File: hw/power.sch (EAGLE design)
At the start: 18 parts, among them U1 TPS54200, U7 MIC5233

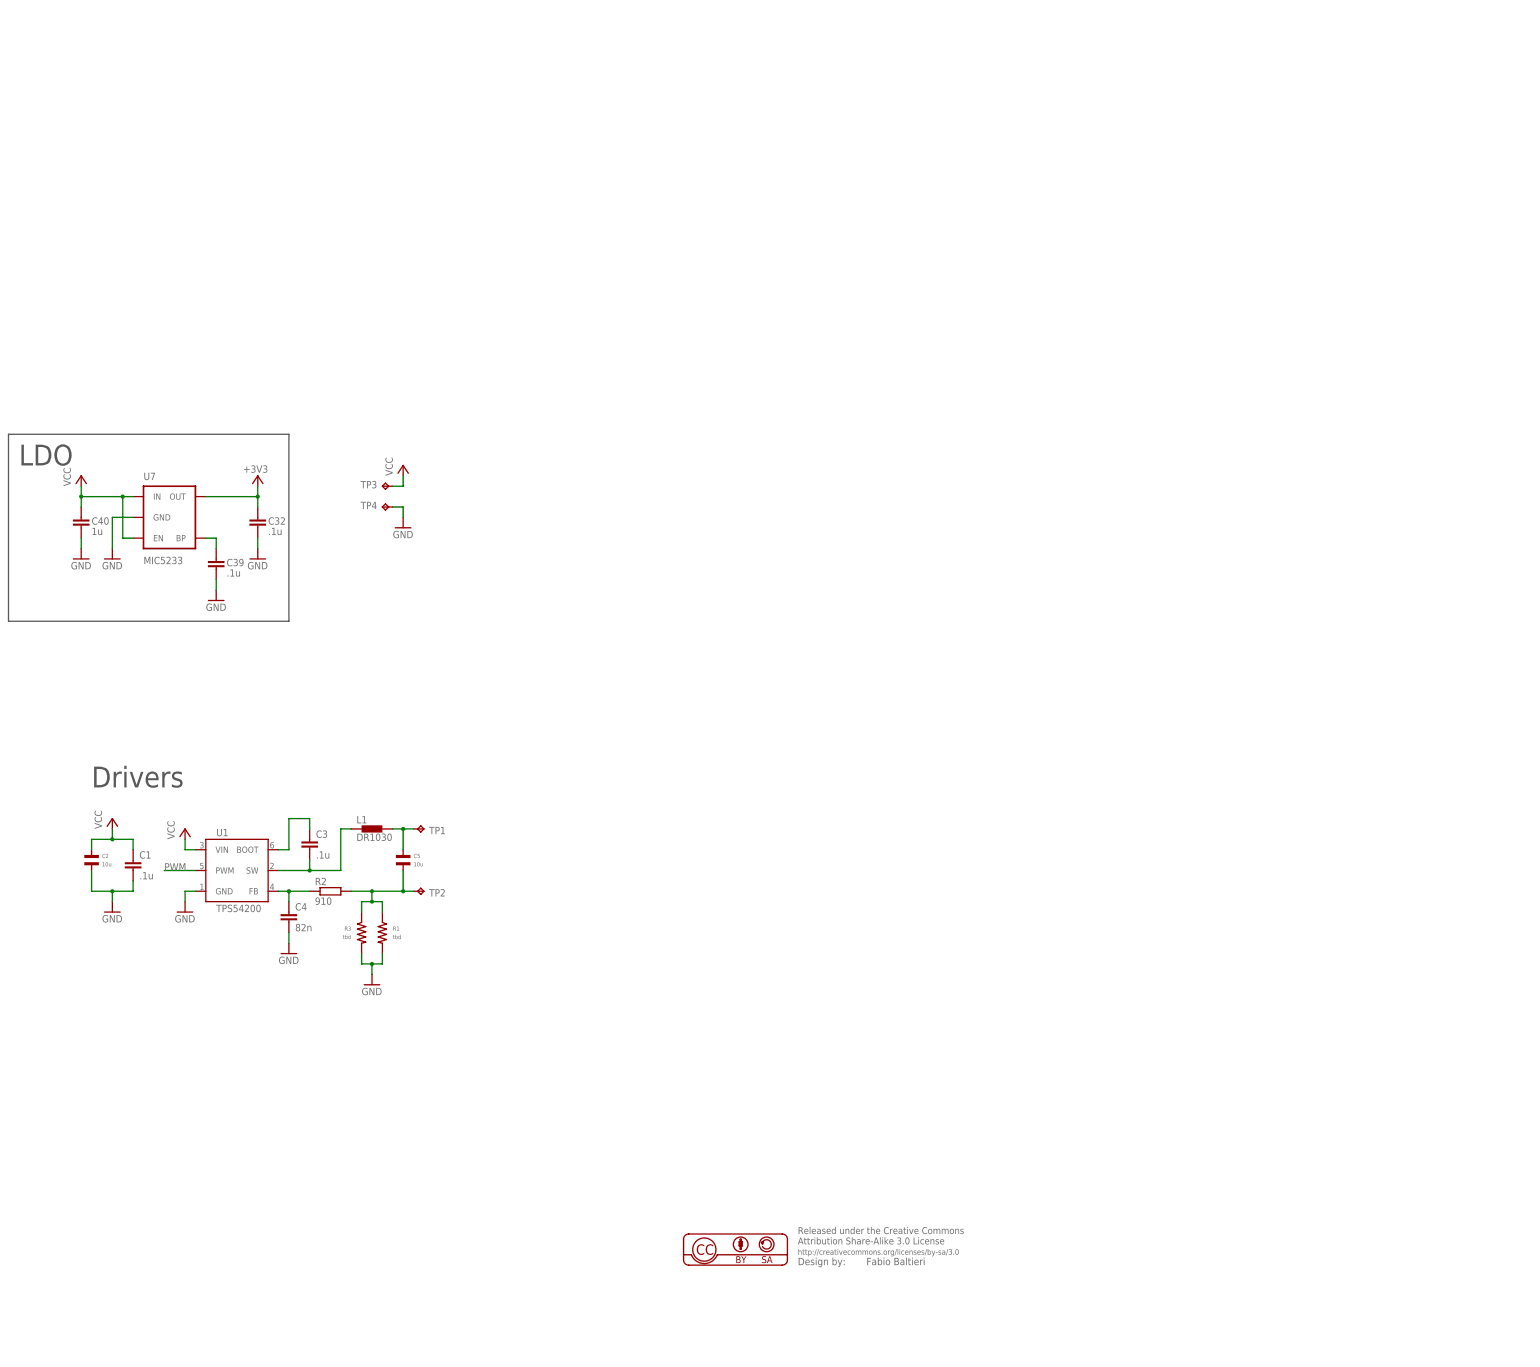
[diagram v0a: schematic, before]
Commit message: power: power routed, control placed
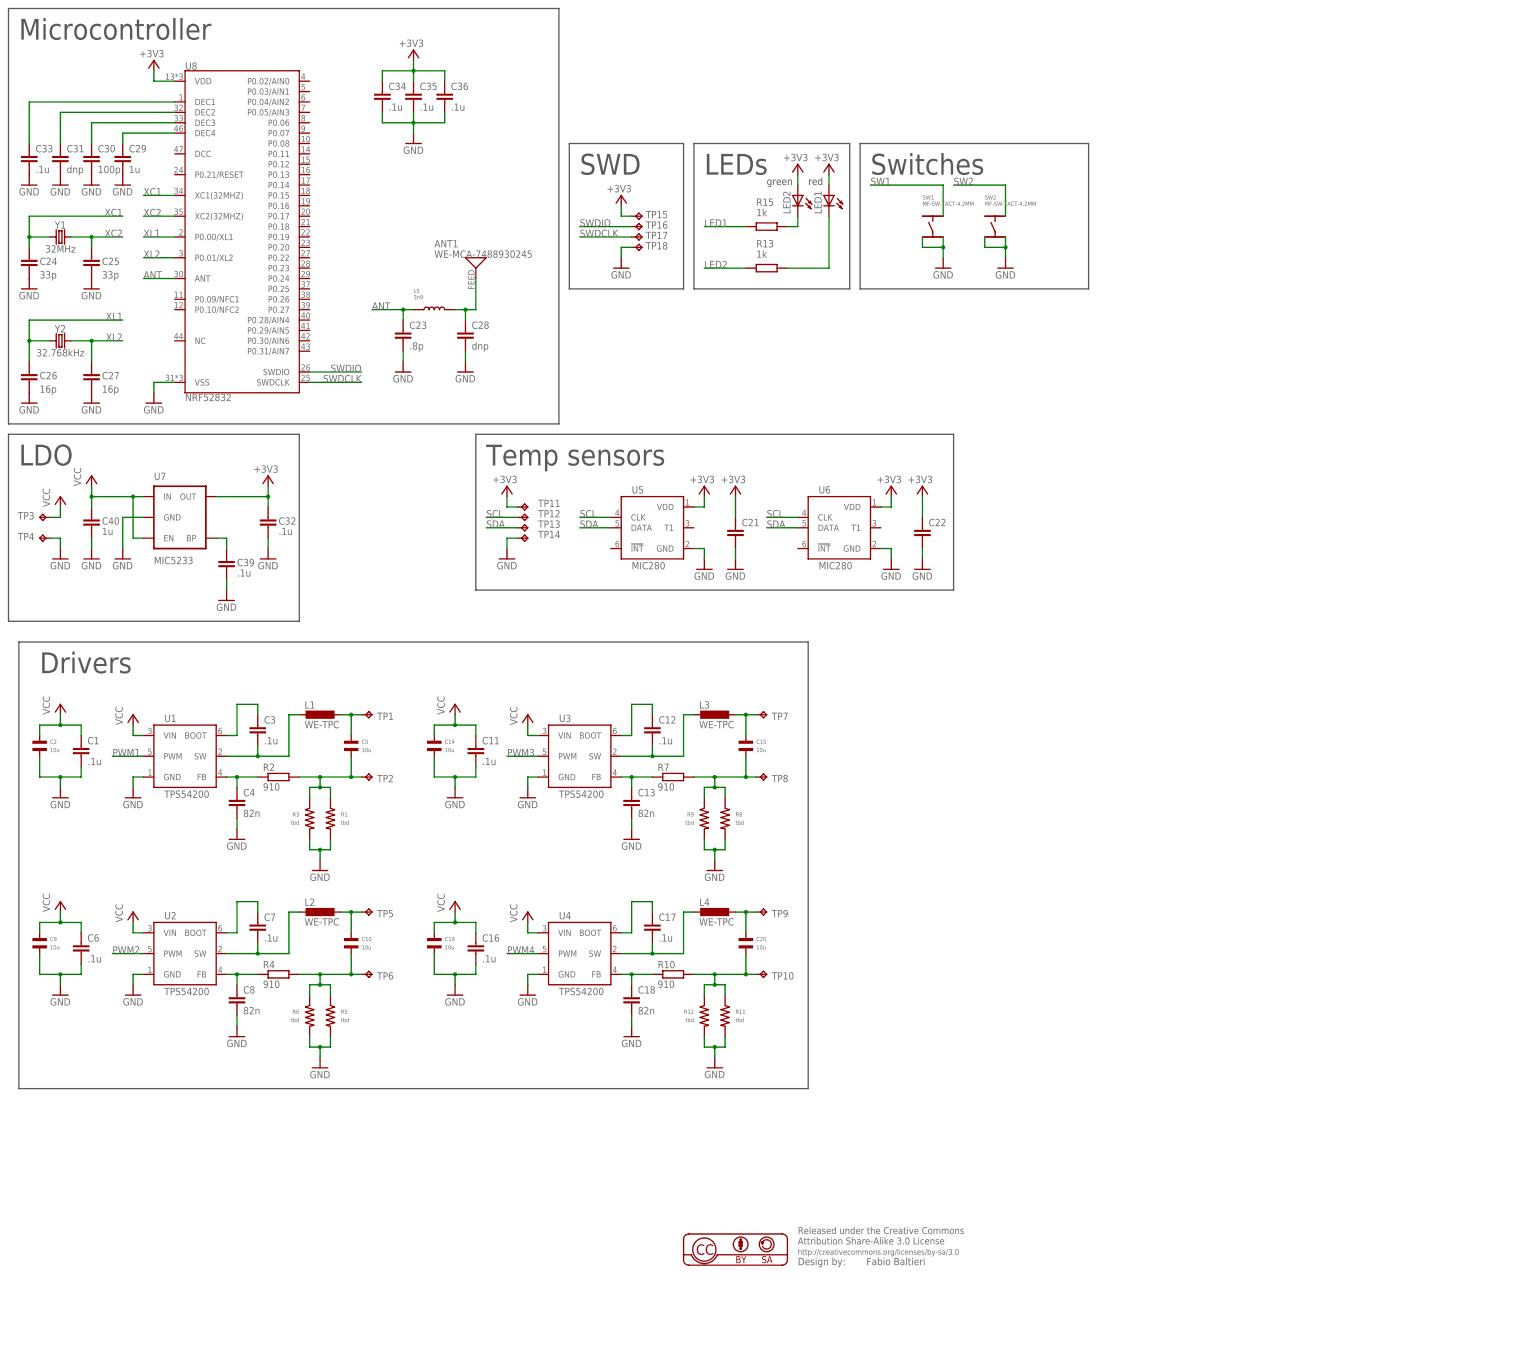
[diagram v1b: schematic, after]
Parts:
- added ANT1: WE-MCA-7488930245, balto:WE-MCA-7488930245
- added C10, C14, C15, C19, C20, C9: 10u, MF_Passives:CAPACITOR_NP_1206
- added C11, C12, C16, C17, C33, C34, C35, C36, C6, C7: .1u, balto:C0603
- added C13, C18, C8: 82n, balto:C0603
- added C21, C22: (no value), balto:C0603
- added C23: .8p, balto:C0603
- added C24, C25: 33p, balto:C0603
- added C26, C27: 16p, balto:C0603
- added C28, C31: dnp, balto:C0603
- added C29: 1u, balto:C0603
- added C30: 100p, balto:C0603
- added L2, L3, L4: WE-TPC, balto:WE-TPC
- added L5: 3n9, MF_Passives:INDUCTOR_0603
- added LED1, LED2: (no value), led:LEDSML0805
- added R10, R4, R7: 910, balto:R0603
- added R11, R12, R5, R6, R8, R9: tbd, MF_Passives:RESISTOR_0805
- added R13, R15: 1k, balto:R0603
- added SW1, SW2: MF-SW-TACT-4.2MM, MF_Switches:TACT_4.2MM
- added TP10, TP5, TP6, TP7, TP8, TP9: TPTP18R, testpad:TPTP18R
- added TP11, TP12, TP13, TP14: TPTP14R, testpad:TPTP14R
- added TP15, TP16, TP17, TP18: TPTP12R, testpad:TPTP12R
- added U2, U3, U4: TPS54200, balto:TPS54200
- added U5, U6: MIC280, balto:MIC280
- added U8: NRF52832, SparkFun-RF:NRF52832
- added Y1: 32MHz, SparkFun-Clocks:CRYSTALSMD-3.2X2.5
- added Y2: 32.768kHz, SparkFun-Clocks:CRYSTAL-32.768KHZSMD-3.2X1.5
- L1: value DR1030 -> WE-TPC; device inductors:DR1030 -> balto:WE-TPC
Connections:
- net PWM renamed PWM1
- new net ANT: C23.1, L5.P$1, U8.ANT
- new net LED1: R15.2
- new net LED2: R13.2
- new net N$10: C10.P$1, L2.2, TP5.TP
- new net N$11: C12.2, L3.1, U3.SW
- new net N$12: C12.1, U3.BOOT
- new net N$13: C13.1, R7.1, U3.FB
- new net N$14: C15.P$2, R7.2, R8.P$1, R9.P$1, TP8.TP
- new net N$15: C15.P$1, L3.2, TP7.TP
- new net N$16: C17.2, L4.1, U4.SW
- new net N$17: C17.1, U4.BOOT
- new net N$18: C18.1, R10.1, U4.FB
- new net N$19: C20.P$2, R10.2, R11.P$1, R12.P$1, TP10.TP
- new net N$20: C20.P$1, L4.2, TP9.TP
- new net N$21: LED1.C, R13.1
- new net N$22: ANT1.P$1, C28.1, L5.P$2
- new net N$23: LED2.C, R15.1
- new net N$24: C29.1, U8.DEC4
- new net N$25: C30.1, U8.DEC3
- new net N$26: C31.1, U8.DEC2
- new net N$27: C33.1, U8.DEC1
- new net N$6: C7.2, L2.1, U2.SW
- new net N$7: C7.1, U2.BOOT
- new net N$8: C8.1, R4.1, U2.FB
- new net N$9: C10.P$2, R4.2, R5.P$1, R6.P$1, TP6.TP
- new net PWM2: U2.PWM
- new net PWM3: U3.PWM
- new net PWM4: U4.PWM
- new net SCL: TP12.TP, U5.CLK, U6.CLK
- new net SDA: TP13.TP, U5.DATA, U6.DATA
- new net SW1: SW1.P$2
- new net SW2: SW2.P$2
- new net SWDCLK: TP17.TP, U8.SWDCLK
- new net SWDIO: TP16.TP, U8.SWDIO
- new net XC1: C24.1, U8.XC1(32MHZ), Y1.1
- new net XC2: C25.1, U8.XC2(32MHZ), Y1.2
- new net XL1: C26.1, U8.P0.00/XL1, Y2.1
- new net XL2: C27.1, U8.P0.01/XL2, Y2.2
- net +3V3: now also C21.1, C22.1, C34.1, C35.1, C36.1, LED1.A, LED2.A, TP11.TP, TP15.TP, U5.VDD, U6.VDD, U8.VDD
- net GND: now also C11.2, C13.2, C14.P$2, C16.2, C18.2, C19.P$2, C21.2, C22.2, C23.2, C24.2, C25.2, C26.2, C27.2, C28.2, C29.2, C30.2, C31.2, C33.2, C34.2, C35.2, C36.2, C6.2, C8.2, C9.P$2, R11.P$2, R12.P$2, R5.P$2, R6.P$2, R8.P$2, R9.P$2, SW1.P$3, SW1.P$4, SW2.P$3, SW2.P$4, TP14.TP, TP18.TP, U2.GND, U3.GND, U4.GND, U5.GND, U6.GND, U8.VSS
- net VCC: now also C11.1, C14.P$1, C16.1, C19.P$1, C6.1, C9.P$1, U2.VIN, U3.VIN, U4.VIN
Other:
- note added: "LEDs"
- note added: "Microcontroller"
- note added: "SWD"
- note added: "Switches"
- note added: "Temp sensors"
- note added: "green"
- note added: "red"
- moved on the sheet: C1, C2, C3, C32, C39, C4, C40, C5, L1, R1, R2, R3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

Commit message: power: r0?
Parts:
- added R14, R16: 5k6, balto:R0603
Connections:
- net +3V3: now also R14.1, R16.1
- net LED1: now also U8.P0.07
- net LED2: now also U8.P0.08
- net PWM1: now also U8.P0.31/AIN7
- net PWM2: now also U8.P0.30/AIN6
- net PWM3: now also U8.P0.29/AIN5
- net PWM4: now also U8.P0.28/AIN4
- net SCL: now also R14.2, U8.P0.27
- net SDA: now also R16.2, U8.P0.26
- net SW1: now also U8.P0.05/AIN3
- net SW2: now also U8.P0.06
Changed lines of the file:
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@@
 <part name="SW2" library="MF_Switches" deviceset="TACT" device="_4.2MM" value="MF-SW-TACT-4.2MM"/>
 <part name="GND37" library="supply1" deviceset="GND" device=""/>
+<part name="R14" library="balto" deviceset="R" device="0603" value="5k6"/>
+<part name="R16" library="balto" deviceset="R" device="0603" value="5k6"/>
+<part name="+3V12" library="supply1" deviceset="+3V3" device=""/>
+<part name="+3V13" library="supply1" deviceset="+3V3" device=""/>
 </parts>
 <sheets>
@@
 <text x="7.62" y="170.18" size="5.08" layer="97">Drivers</text>
 <wire x1="114.3" y1="190.5" x2="114.3" y2="228.6" width="0.1524" layer="97"/>
-<wire x1="114.3" y1="228.6" x2="231.14" y2="228.6" width="0.1524" layer="97"/>
-<wire x1="231.14" y1="228.6" x2="231.14" y2="190.5" width="0.1524" layer="97"/>
-<wire x1="231.14" y1="190.5" x2="114.3" y2="190.5" width="0.1524" layer="97"/>
+<wire x1="114.3" y1="228.6" x2="256.54" y2="228.6" width="0.1524" layer="97"/>
+<wire x1="256.54" y1="228.6" x2="256.54" y2="190.5" width="0.1524" layer="97"/>
+<wire x1="256.54" y1="190.5" x2="114.3" y2="190.5" width="0.1524" layer="97"/>
 <text x="116.84" y="220.98" size="5.08" layer="97">Temp sensors</text>
 <wire x1="2.54" y1="177.8" x2="195.58" y2="177.8" width="0.1524" layer="97"/>
@@
 <instance part="SW2" gate="G$1" x="241.3" y="279.4"/>
 <instance part="GND37" gate="1" x="243.84" y="269.24"/>
+<instance part="R14" gate="G$1" x="238.76" y="205.74" smashed="yes" rot="R270">
+<attribute name="NAME" x="241.3" y="205.74" size="1.778" layer="95"/>
+<attribute name="VALUE" x="241.3" y="203.2" size="1.778" layer="96"/>
+</instance>
+<instance part="R16" gate="G$1" x="248.92" y="205.74" smashed="yes" rot="R270">
+<attribute name="NAME" x="251.46" y="205.74" size="1.778" layer="95"/>
+<attribute name="VALUE" x="251.46" y="203.2" size="1.778" layer="96"/>
+</instance>
+<instance part="+3V12" gate="G$1" x="238.76" y="215.9" smashed="yes">
+<attribute name="VALUE" x="241.3" y="218.44" size="1.778" layer="96" rot="R180"/>
+</instance>
+<instance part="+3V13" gate="G$1" x="248.92" y="215.9" smashed="yes">
+<attribute name="VALUE" x="251.46" y="218.44" size="1.778" layer="96" rot="R180"/>
+</instance>
 </instances>
 <busses>
@@
 <pinref part="+3V10" gate="G$1" pin="+3V3"/>
 <wire x1="200.66" y1="289.56" x2="200.66" y2="292.1" width="0.1524" layer="91"/>
+</segment>
+<segment>
+<pinref part="R14" gate="G$1" pin="1"/>
+<pinref part="+3V12" gate="G$1" pin="+3V3"/>
+<wire x1="238.76" y1="210.82" x2="238.76" y2="213.36" width="0.1524" layer="91"/>
+</segment>
+<segment>
+<pinref part="R16" gate="G$1" pin="1"/>
+<pinref part="+3V13" gate="G$1" pin="+3V3"/>
+<wire x1="248.92" y1="210.82" x2="248.92" y2="213.36" width="0.1524" layer="91"/>
 </segment>
 </net>
@@
 <wire x1="129.54" y1="101.6" x2="121.92" y2="101.6" width="0.1524" layer="91"/>
 <label x="121.92" y="101.6" size="1.778" layer="95"/>
+</segment>
+<segment>
+<pinref part="U8" gate="G$1" pin="P0.28/AIN4"/>
+<wire x1="83.82" y1="256.54" x2="73.66" y2="256.54" width="0.1524" layer="91"/>
+<label x="83.82" y="256.54" size="1.778" layer="95" rot="MR0"/>
 </segment>
 </net>
@@
 <label x="116.84" y="208.28" size="1.778" layer="95"/>
 </segment>
+<segment>
+<pinref part="U8" gate="G$1" pin="P0.27"/>
+<wire x1="73.66" y1="259.08" x2="83.82" y2="259.08" width="0.1524" layer="91"/>
+<label x="83.82" y="259.08" size="1.778" layer="95" rot="MR0"/>
+</segment>
+<segment>
+<wire x1="231.14" y1="198.12" x2="238.76" y2="198.12" width="0.1524" layer="91"/>
+<pinref part="R14" gate="G$1" pin="2"/>
+<wire x1="238.76" y1="198.12" x2="238.76" y2="200.66" width="0.1524" layer="91"/>
+<label x="231.14" y="198.12" size="1.778" layer="95"/>
+</segment>
 </net>
 <net name="SDA" class="0">
@@
 <label x="116.84" y="205.74" size="1.778" layer="95"/>
 </segment>
+<segment>
+<pinref part="U8" gate="G$1" pin="P0.26"/>
+<wire x1="83.82" y1="261.62" x2="73.66" y2="261.62" width="0.1524" layer="91"/>
+<label x="83.82" y="261.62" size="1.778" layer="95" rot="MR0"/>
+</segment>
+<segment>
+<pinref part="R16" gate="G$1" pin="2"/>
+<wire x1="231.14" y1="195.58" x2="248.92" y2="195.58" width="0.1524" layer="91"/>
+<wire x1="248.92" y1="195.58" x2="248.92" y2="200.66" width="0.1524" layer="91"/>
+<label x="231.14" y="195.58" size="1.778" layer="95"/>
+</segment>
 </net>
 <net name="PWM1" class="0">
@@
 <label x="25.4" y="149.86" size="1.778" layer="95"/>
 </segment>
+<segment>
+<pinref part="U8" gate="G$1" pin="P0.31/AIN7"/>
+<wire x1="73.66" y1="248.92" x2="83.82" y2="248.92" width="0.1524" layer="91"/>
+<label x="83.82" y="248.92" size="1.778" layer="95" rot="MR0"/>
+</segment>
 </net>
 <net name="PWM2" class="0">
@@
 <label x="25.4" y="101.6" size="1.778" layer="95"/>
 </segment>
+<segment>
+<pinref part="U8" gate="G$1" pin="P0.30/AIN6"/>
+<wire x1="83.82" y1="251.46" x2="73.66" y2="251.46" width="0.1524" layer="91"/>
+<label x="83.82" y="251.46" size="1.778" layer="95" rot="MR0"/>
+</segment>
 </net>
 <net name="PWM3" class="0">
@@
 <wire x1="129.54" y1="149.86" x2="121.92" y2="149.86" width="0.1524" layer="91"/>
 <label x="121.92" y="149.86" size="1.778" layer="95"/>
+</segment>
+<segment>
+<pinref part="U8" gate="G$1" pin="P0.29/AIN5"/>
+<wire x1="73.66" y1="254" x2="83.82" y2="254" width="0.1524" layer="91"/>
+<label x="83.82" y="254" size="1.778" layer="95" rot="MR0"/>
 </segment>
 </net>
@@
 <wire x1="228.6" y1="281.94" x2="228.6" y2="289.56" width="0.1524" layer="91"/>
 </segment>
+<segment>
+<pinref part="U8" gate="G$1" pin="P0.05/AIN3"/>
+<wire x1="83.82" y1="307.34" x2="73.66" y2="307.34" width="0.1524" layer="91"/>
+<label x="83.82" y="307.34" size="1.778" layer="95" rot="MR0"/>
+</segment>
 </net>
 <net name="LED1" class="0">
@@
 <label x="170.18" y="279.4" size="1.778" layer="95"/>
 </segment>
+<segment>
+<pinref part="U8" gate="G$1" pin="P0.07"/>
+<wire x1="83.82" y1="302.26" x2="73.66" y2="302.26" width="0.1524" layer="91"/>
+<label x="83.82" y="302.26" size="1.778" layer="95" rot="MR0"/>
+</segment>
 </net>
 <net name="LED2" class="0">
@@
 <wire x1="180.34" y1="269.24" x2="170.18" y2="269.24" width="0.1524" layer="91"/>
 <label x="170.18" y="269.24" size="1.778" layer="95"/>
+</segment>
+<segment>
+<pinref part="U8" gate="G$1" pin="P0.08"/>
+<wire x1="73.66" y1="299.72" x2="83.82" y2="299.72" width="0.1524" layer="91"/>
+<label x="83.82" y="299.72" size="1.778" layer="95" rot="MR0"/>
 </segment>
 </net>
@@
 <label x="231.14" y="289.56" size="1.778" layer="95"/>
 </segment>
-</net>
+<segment>
+<pinref part="U8" gate="G$1" pin="P0.06"/>
+<wire x1="73.66" y1="304.8" x2="83.82" y2="304.8" width="0.1524" layer="91"/>
+<label x="83.82" y="304.8" size="1.778" layer="95" rot="MR0"/>
+</segment>
+</net>
